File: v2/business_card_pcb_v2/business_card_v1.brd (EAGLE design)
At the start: 89 x 51 mm, 75 parts, among them SW1 SPST_TACT-KMR2

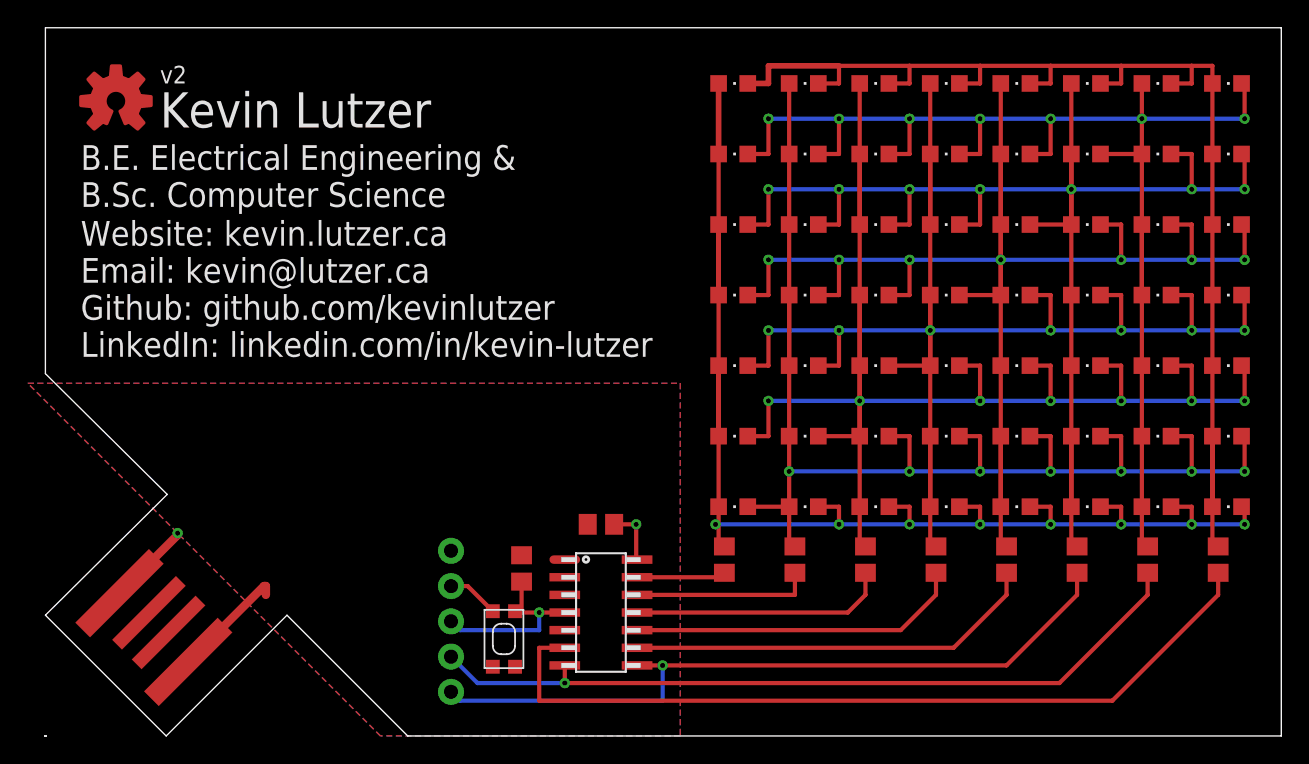
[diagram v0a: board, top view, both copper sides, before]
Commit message: add the sck pad pin for miso and mosi
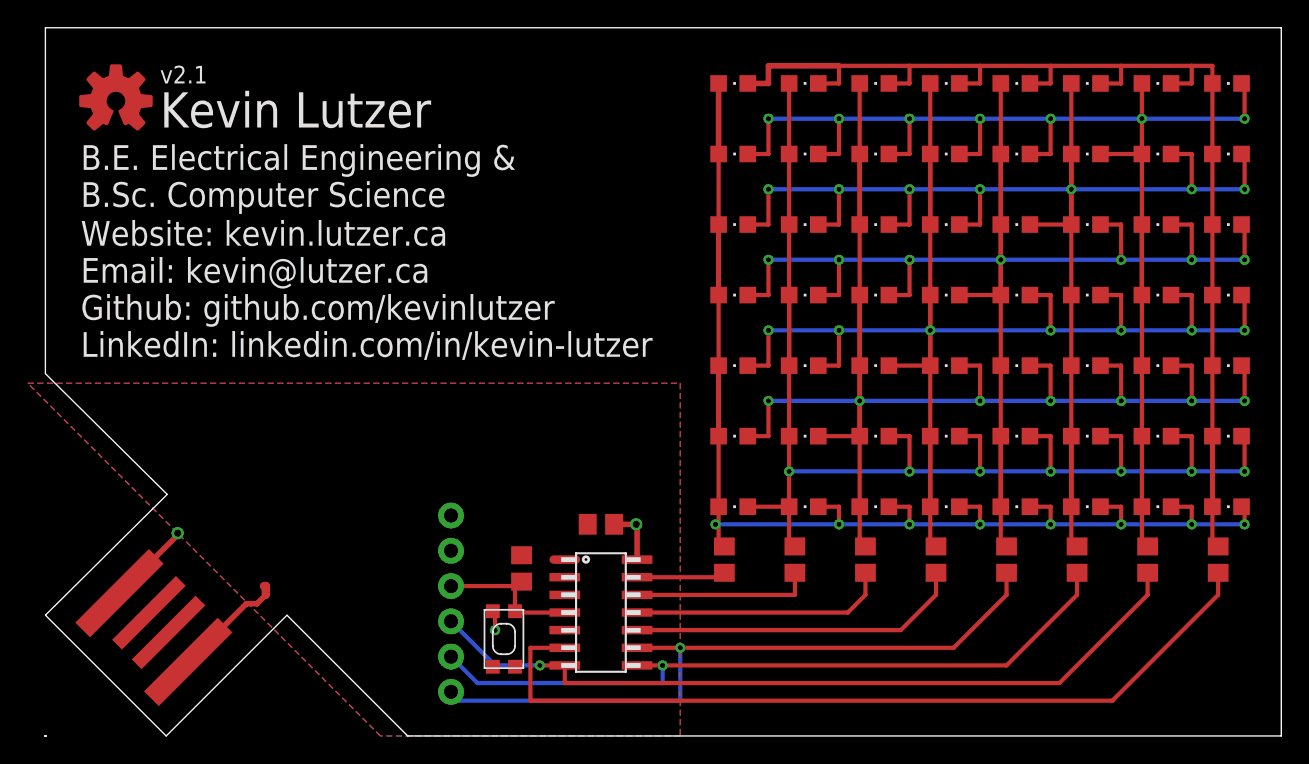
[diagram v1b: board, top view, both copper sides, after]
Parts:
- added TP6: TEST-POINTPOGO_PTH, SparkFun-Connectors:1X01_NO_SILK
- added U$2, U$3: (no value), adafruit:OSHWLOGO_TOL_0.2
- moved TP4 2.54 mm to (29.2, 8.26)
- moved TP5 2.54 mm to (29.2, 13.3)
- moved TP2 2.54 mm to (29.2, 5.71)
- moved TP1 2.54 mm to (29.2, 10.8)
- moved TP3 2.54 mm to (29.2, 15.9)
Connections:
- net PIN5 renamed MISO
- net PIN6 renamed MOSI
- removed net PIN4: IC1.9, R6.1
- new net SCK: IC1.9, R6.1, TP6.1
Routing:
- net SCK: track 0.00 -> 50.4 mm, vias 0 -> 1
- net PIN4: track 29.8 -> 0.00 mm
- net RESET: track 13.7 -> 11.2 mm, vias 1 -> 0
- net GND: track 14.0 -> 11.7 mm, vias 2 -> 3
- net PIN7: track 59.3 -> 60.6 mm
- net MISO: track 53.4 -> 52.7 mm
- net MOSI: track 56.4 -> 57.1 mm
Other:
- board text added: "v2.1"
- board text removed: "v2"
